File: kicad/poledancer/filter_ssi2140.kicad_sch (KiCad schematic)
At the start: 93 parts, among them U10 AS3364, U11 TL074, U12 SSI2140, U13 SSI2190, U14 TL074, U15 DG442xY, U3 TL074

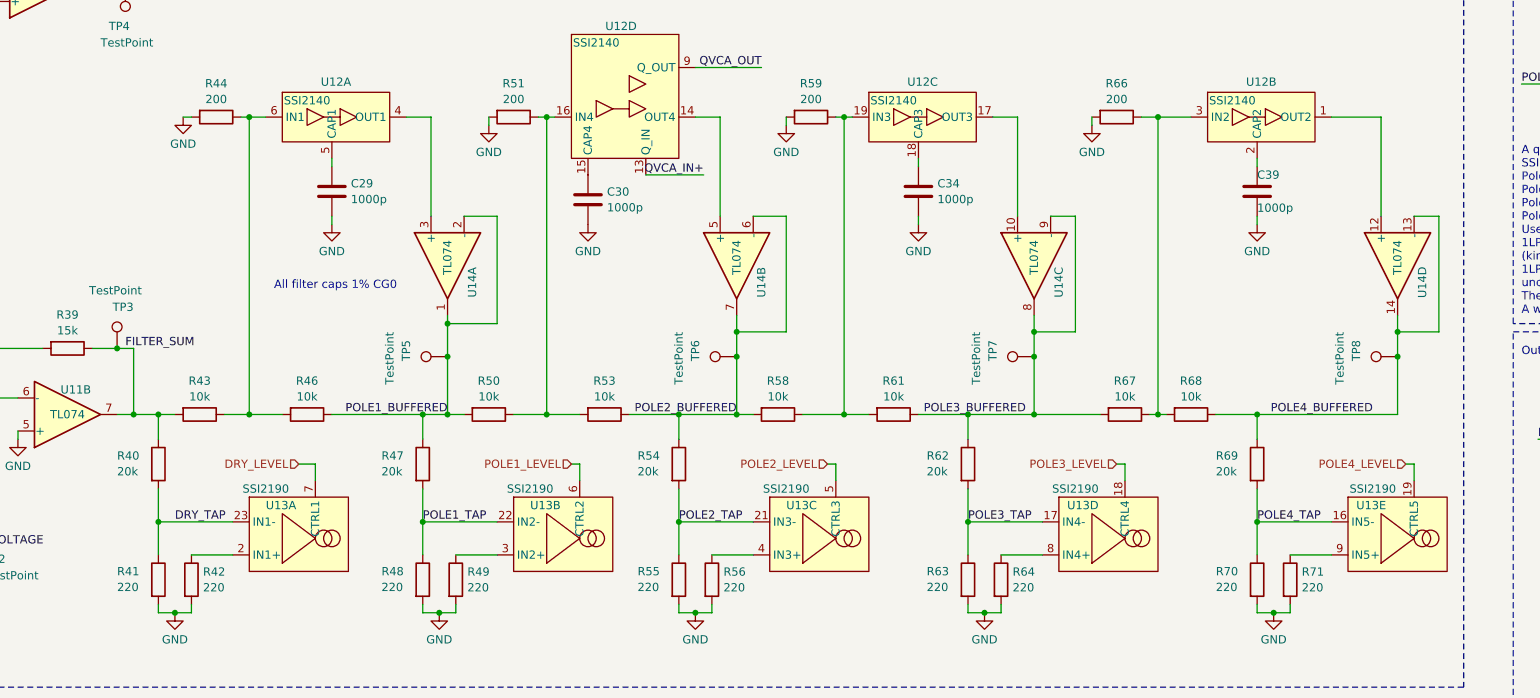
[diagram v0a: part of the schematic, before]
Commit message: create hand solder footprints for SSI chips.  Get some placement done.
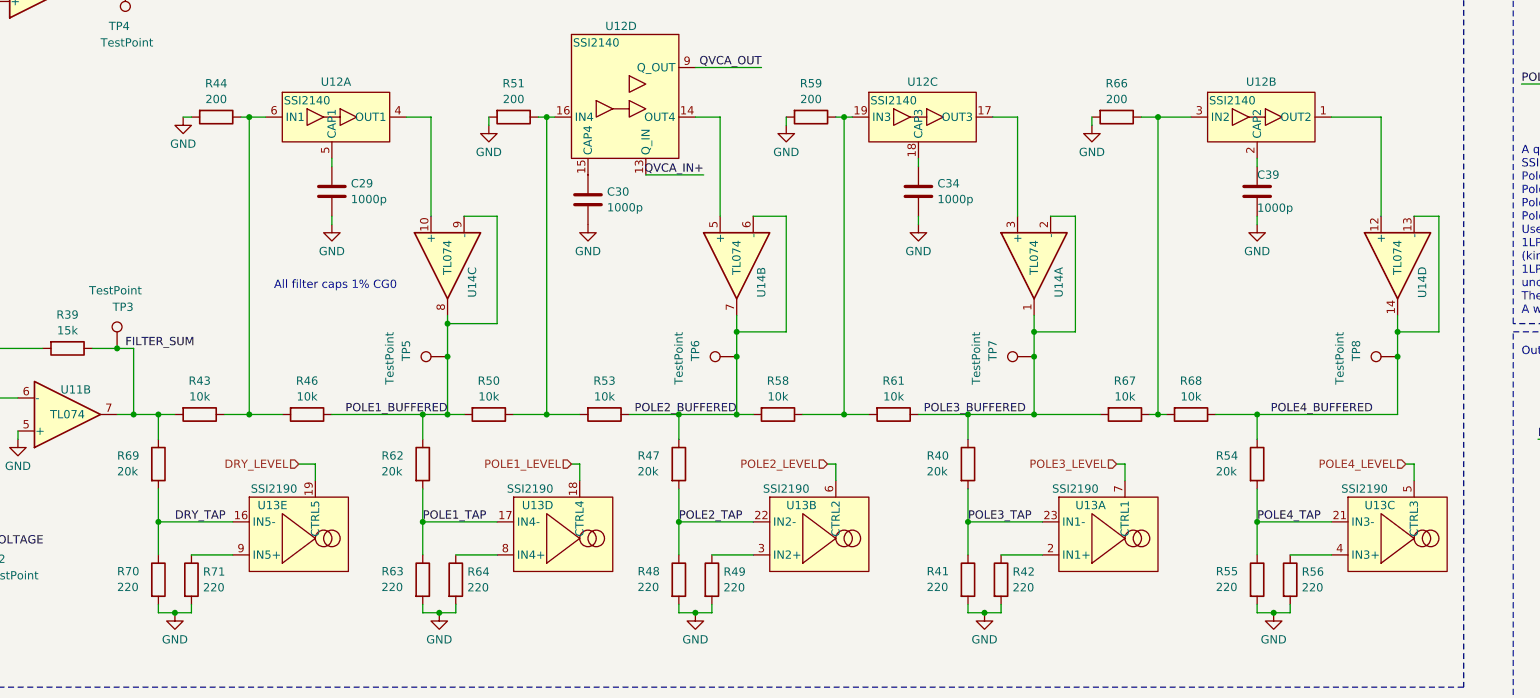
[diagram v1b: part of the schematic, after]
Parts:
- C29, C30, C34, C39: footprint Capacitor_SMD:C_1206_3216Metric -> Capacitor_SMD:C_0805_2012Metric; Digikey 311-1911-1-ND -> 478-KGM21BCG1H102FTCT-ND; Mfg CC1206FRNPO9BN102 -> KGM21BCG1H102FT
- U12: footprint Package_SO:SSOP-20_3.9x8.7mm_P0.635mm -> project_footprints:SSOP-20_3.9x8.7mm_P0.635mm_HandSolder
- U13: footprint Package_SO:SSOP-24_3.9x8.7mm_P0.635mm -> project_footprints:SSOP-24_3.9x8.7mm_P0.635mm_HandSolder
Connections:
- net DRY_LEVEL: now also U13.19 (CTRL5); no longer U13.7 (CTRL1)
- net DRY_TAP: now also R69.2, R70.1, U13.16 (IN5-); no longer R40.2, R41.1, U13.23 (IN1-)
- net FILTER_SUM: now also R69.1; no longer R40.1
- net POLE1_BUFFERED: now also R62.1, U14.8, U14.9 (-); no longer R47.1, U14.1, U14.2 (-)
- net POLE1_LEVEL: now also U13.18 (CTRL4); no longer U13.6 (CTRL2)
- net POLE1_TAP: now also R62.2, R63.1, U13.17 (IN4-); no longer R47.2, R48.1, U13.22 (IN2-)
- net POLE2_BUFFERED: now also R47.1; no longer R54.1
- net POLE2_LEVEL: now also U13.6 (CTRL2); no longer U13.5 (CTRL3)
- net POLE2_TAP: now also R47.2, R48.1, U13.22 (IN2-); no longer R54.2, R55.1, U13.21 (IN3-)
- net POLE3_BUFFERED: now also R40.1, U14.1, U14.2 (-); no longer R62.1, U14.8, U14.9 (-)
- net POLE3_LEVEL: now also U13.7 (CTRL1); no longer U13.18 (CTRL4)
- net POLE3_TAP: now also R40.2, R41.1, U13.23 (IN1-); no longer R62.2, R63.1, U13.17 (IN4-)
- net POLE4_BUFFERED: now also R54.1; no longer R69.1
- net POLE4_LEVEL: now also U13.5 (CTRL3); no longer U13.19 (CTRL5)
- net POLE4_TAP: now also R54.2, R55.1, U13.21 (IN3-); no longer R69.2, R70.1, U13.16 (IN5-)
- net at U12.4 (OUT1): now also U14.10 (+); no longer U14.3 (+)
- net at U12.17 (OUT3): now also U14.3 (+); no longer U14.10 (+)
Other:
- moved on the sheet: R40, R41, R42, R47, R48, R49, R54, R55, R56, R62, R63, R64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

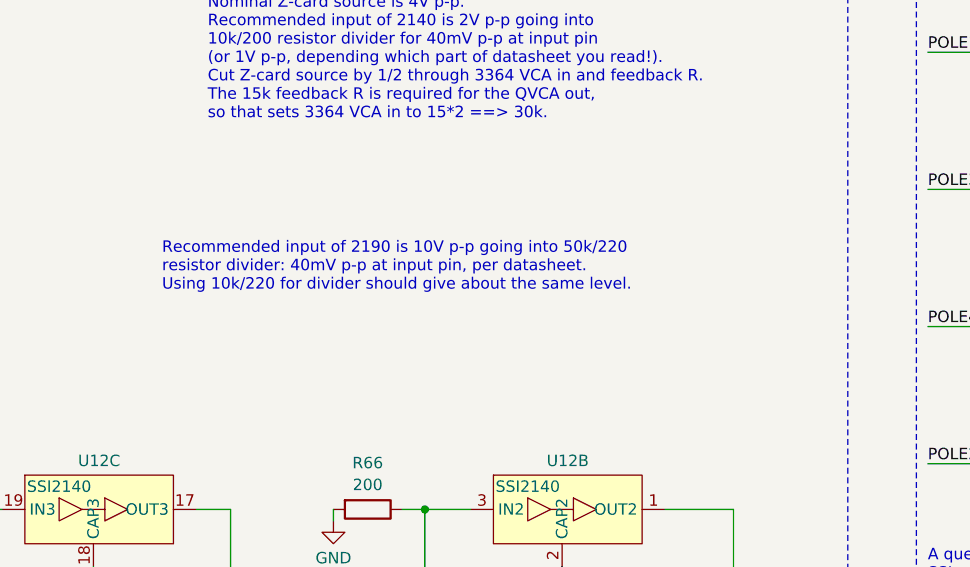
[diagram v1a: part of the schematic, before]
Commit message: checkpoint before changing some direction on this.  The resonance compensation is completely bonkers wrong.  Need to address that.
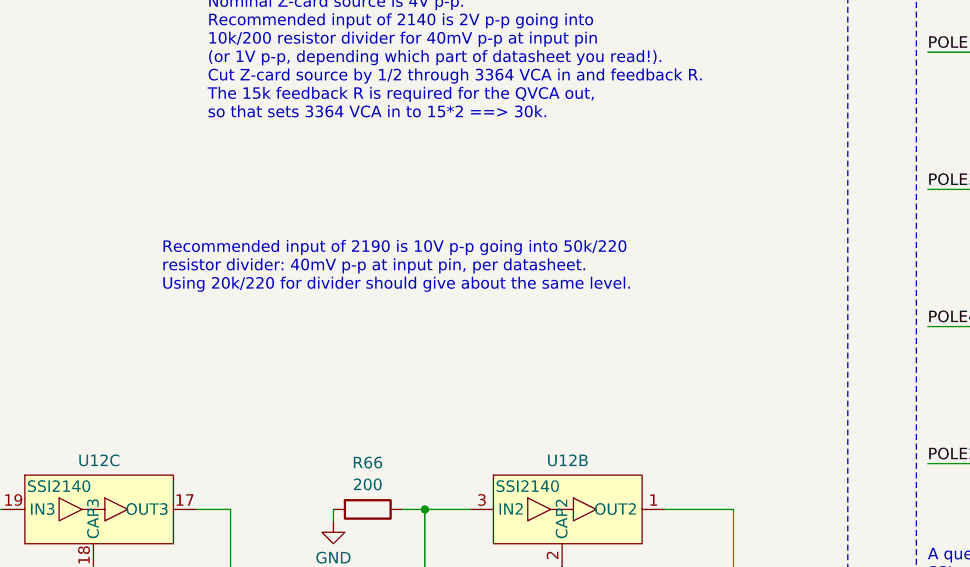
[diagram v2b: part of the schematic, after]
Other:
- note added: "Recommended input of 2190 is 10V p-p going into 50k/220 resistor divider: 40mV p-p at input pin, per datasheet. Using 20k/220 for divider should give about the same level."
- note removed: "Recommended input of 2190 is 10V p-p going into 50k/220 resistor divider: 40mV p-p at input pin, per datasheet. Using 10k/220 for divider should give about the same level."
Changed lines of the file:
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@@
     (effects (font (size 1.27 1.27)) (justify left bottom))
   )
-  (text "Recommended input of 2190 is 10V p-p going into 50k/220\nresistor divider: 40mV p-p at input pin, per datasheet.\nUsing 10k/220 for divider should give about the same level.\n"
+  (text "Recommended input of 2190 is 10V p-p going into 50k/220\nresistor divider: 40mV p-p at input pin, per datasheet.\nUsing 20k/220 for divider should give about the same level.\n"
     (at 234.95 52.07 0)
     (effects (font (size 1.27 1.27)) (justify left bottom))

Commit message: updated rez comp mode.  Back to placement on PCB.
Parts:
- removed R78: 20k, Resistor_SMD:R_0603_1608Metric, symbol Device:R
- R26: value 20k -> 15k; LCSC C4184 -> C22809
- R75: value 20k -> 10k; LCSC C4184 -> (none)
- U13: footprint project_footprints:SSOP-24_3.9x8.7mm_P0.635mm_HandSolder -> Package_SO:SSOP-24_3.9x8.7mm_P0.635mm
- renumbered R58 to R50, R50 to R58
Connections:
- net REZ_STAGE4_ENABLE is gone; now on net REZ_STAGE3_ENABLE: U15.16
- net GND: now also U11.12 (+); no longer R26.1, U11.5 (+)
- net POLE2_BUFFERED: now also R74.2
- net POLE3_BUFFERED: now also R75.2; no longer R74.2
- net POLE4_BUFFERED: no longer R75.2
- net QVCA_VOLTAGE: now also R26.2
- net REZ_STAGE2_ENABLE: now also U15.9; no longer U15.8
- net REZ_STAGE3_ENABLE: no longer U15.9
- net SOURCE1_AUDIO_LEVEL: now also U10.14 (Vc); no longer U10.3 (Vc)
- net SOURCE1_MOD_LEVEL: now also U10.3 (Vc); no longer U10.11 (Vc)
- net SOURCE2_AUDIO_LEVEL: now also U10.11 (Vc); no longer U10.6 (Vc)
- net SOURCE2_MOD_LEVEL: now also U10.6 (Vc); no longer U10.14 (Vc)
- net at U12.1 (OUT2): now also U14.5 (+); no longer U14.12 (+)
- net at U12.2 (CAP2): now also C30.1; no longer C39.1
- net at R66.1, R67.1, R68.2: now also U12.16 (IN4); no longer U12.3 (IN2)
- net at C28.1, R36.1, R38.2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: now also U10.4 (Iout), U10.5 (Iout); no longer U10.12 (Iout), U10.13 (Iout)
- net at R33.2: now also U10.15 (Iin); no longer U10.2 (Iin)
- net at U12.14 (OUT4): now also U14.12 (+); no longer U14.5 (+)
- net at R32.2: now also U10.7 (Iin); no longer U10.15 (Iin)
- net at U12.15 (CAP4): now also C39.1; no longer C30.1
- net at R34.2: now also U10.10 (Iin); no longer U10.7 (Iin)
- net at R37.1, R39.2, U11.6 (-): now also U10.12 (Iout), U10.13 (Iout); no longer U10.4 (Iout), U10.5 (Iout)
- net at R51.1, R53.2, R58.1: now also U12.3 (IN2); no longer U12.16 (IN4)
- net at R31.2: now also U10.2 (Iin); no longer U10.10 (Iin)
- new net: R26.1, U11.5 (+), U15.6
- new net QVCA_INVERT: U15.8
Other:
- note added: "A couple things on that opamp U11B... 15k is useful as the I-to-V for the 3364 VCA outputs. So 15k all around. The QVCA input can be switched phase based on the invert switch. This works as a summing only because the 3364 is current output, not voltage."
- note added: "A questionably weighted selection is used for resonance compensation. SSI app note AN701 details using SSI2164. This attempts the concept. Pole 1 switchable with a weight of 1. Pole 2 switchable with a weight of 1. Pole 3 switchable with a weight of 2. Pole 4 hardwired in the 2140 with a weight of 1. Used in conjuntion with QVCA_INVERT to phase correct the output. Useful combinations in the form 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"
- note added: "Sheet Vref load: 24k"
- note removed: "A questionably weighted selection is used for resonance compensation. SSI app note AN701 details using SSI2164. This attempts the concept. Pole 1 switchable with a weight of 1. Pole 2 switchable with a weight of 1. Pole 3 switchable with a weight of 1. Pole 4 switchable with a weight of 1. Useful combinations in the form (weight pole 1, 2, 3, 4): 1LP, 1HP: 1, 1, 0, 0 (REZ_STAGE1, STAGE2 set) (kin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"
- moved on the sheet: C30, C39, C42, C43, R35, R37, R73, R74, R75, TP2, U10B, U10C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

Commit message: continue placement
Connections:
- net FILTER_SUM: now also U11.1; no longer U11.7
- net GND: now also U11.5 (+); no longer U11.3 (+)
- net QVCA_OUT: now also U11.6 (-); no longer U11.2 (-)
- net QVCA_VOLTAGE: now also U11.7; no longer U11.1
- net at C28.1, R38.2, U10.4 (Iout)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: now also RV2.3; no longer R36.1
- net at R26.1, U15.6: now also U11.3 (+); no longer U11.5 (+)
- net at R37.1, R39.2, U10.12 (Iout)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: now also U11.2 (-); no longer U11.6 (-)
- net at C25.1, R27.1: now also R36.2; no longer RV2.1, RV2.2
- new net: R36.1, RV2.1, RV2.2
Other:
- moved on the sheet: R36, RV2, U11A, U11B
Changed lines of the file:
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@@
   (junction (at 336.55 181.61) (diameter 0) (color 0 0 0 0)
   )
-  (junction (at 63.5 24.13) (diameter 0) (color 0 0 0 0)
-  )
   (junction (at 154.94 113.03) (diameter 0) (color 0 0 0 0)
   )
@@
   (junction (at 260.35 243.84) (diameter 0) (color 0 0 0 0)
   )
+  (junction (at 71.12 24.13) (diameter 0) (color 0 0 0 0)
+  )
   (junction (at 153.67 152.4) (diameter 0) (color 0 0 0 0)
   )
@@
     (stroke (width 0) (type default))
   )
-  (wire (pts (xy 81.28 24.13) (xy 82.55 24.13))
+  (wire (pts (xy 80.01 24.13) (xy 82.55 24.13))
     (stroke (width 0) (type default))
   )
@@
     (stroke (width 0) (type default))
   )
-  (wire (pts (xy 72.39 24.13) (xy 73.66 24.13))
-    (stroke (width 0) (type default))
-  )
   (wire (pts (xy 238.76 224.79) (xy 238.76 223.52))
     (stroke (width 0) (type default))
@@
     (stroke (width 0) (type default))
   )
-  (wire (pts (xy 68.58 19.05) (xy 63.5 19.05))
+  (wire (pts (xy 76.2 19.05) (xy 71.12 19.05))
     (stroke (width 0) (type default))
   )
@@
     (stroke (width 0) (type default))
   )
-  (wire (pts (xy 68.58 20.32) (xy 68.58 19.05))
+  (wire (pts (xy 76.2 20.32) (xy 76.2 19.05))
     (stroke (width 0) (type default))
   )
@@
     (stroke (width 0) (type default))
   )
-  (wire (pts (xy 63.5 24.13) (xy 64.77 24.13))
+  (wire (pts (xy 71.12 24.13) (xy 72.39 24.13))
     (stroke (width 0) (type default))
   )
@@
     (stroke (width 0) (type default))
   )
-  (wire (pts (xy 63.5 19.05) (xy 63.5 24.13))
+  (wire (pts (xy 71.12 19.05) (xy 71.12 24.13))
     (stroke (width 0) (type default))
   )
@@
     (stroke (width 0) (type default))
   )
+  (wire (pts (xy 70.485 24.13) (xy 71.12 24.13))
+    (stroke (width 0) (type default))
+  )
   (wire (pts (xy 350.52 165.1) (xy 356.87 165.1))
     (stroke (width 0) (type default))
@@
     (stroke (width 0) (type default))
   )
-  (wire (pts (xy 34.29 209.55) (xy 36.83 209.55))
+  (wire (pts (xy 31.115 209.55) (xy 36.83 209.55))
     (stroke (width 0) (type default))
   )
@@
     (stroke (width 0) (type default))
   )
-  (wire (pts (xy 55.88 24.13) (xy 63.5 24.13))
+  (wire (pts (xy 55.88 24.13) (xy 62.865 24.13))
     (stroke (width 0) (type default))
   )
@@
     (effects (font (size 1.27 1.27)) (justify left bottom))
   )
-  (text "OFFSET" (at 34.925 218.44 0)
+  (text "OFFSET" (at 36.195 218.44 0)
     (effects (font (size 1.27 1.27)) (justify left bottom))
   )
@@
     (effects (font (size 1.27 1.27)) (justify left bottom))
   )
-  (text "SCALING" (at 65.405 33.02 0)
+  (text "SCALING" (at 71.12 33.02 0)
     (effects (font (size 1.27 1.27)) (justify left bottom))
   )
@@
     (effects (font (size 1.27 1.27)) (justify right))
   )
-  (hierarchical_label "V2.5_REF" (shape input) (at 34.29 209.55 180) (fields_autoplaced)
+  (hierarchical_label "V2.5_REF" (shape input) (at 31.115 209.55 180) (fields_autoplaced)
     (effects (font (size 1.27 1.27)) (justify right))
   )
@@
     )
   )
-  (symbol (lib_id "Amplifier_Operational:TL074") (at 51.435 142.24 0) (mirror x) (unit 1)
+  (symbol (lib_id "Amplifier_Operational:TL074") (at 96.52 121.92 0) (mirror x) (unit 1)
     (in_bom yes) (on_board yes) (dnp no)
-    (property "Reference" "U11" (at 53.975 138.43 0)
+    (property "Reference" "U11" (at 99.06 118.11 0)
       (effects (font (size 1.27 1.27)))
     )
-    (property "Value" "TL074" (at 50.165 142.24 0)
+    (property "Value" "TL074" (at 95.25 121.92 0)
       (effects (font (size 1.27 1.27)))
     )
-    (property "Footprint" "Package_SO:TSSOP-14_4.4x5mm_P0.65mm" (at 50.165 144.78 0)
+    (property "Footprint" "Package_SO:TSSOP-14_4.4x5mm_P0.65mm" (at 95.25 124.46 0)
       (effects (font (size 1.27 1.27)) hide)
     )
-    (property "Datasheet" "http://www.ti.com/lit/ds/symlink/tl071.pdf" (at 52.705 147.32 0)
+    (property "Datasheet" "http://www.ti.com/lit/ds/symlink/tl071.pdf" (at 97.79 127 0)
       (effects (font (size 1.27 1.27)) hide)
     )
-    (property "LCSC" "C96507" (at 51.435 142.24 0)
+    (property "LCSC" "C96507" (at 96.52 121.92 0)
       (effects (font (size 1.27 1.27)) hide)
     )
@@
     )
   )
-  (symbol (lib_id "Device:R") (at 77.47 24.13 270) (unit 1)
+  (symbol (lib_id "Device:R") (at 66.675 24.13 270) (unit 1)
     (in_bom yes) (on_board yes) (dnp no)
-    (property "Reference" "R36" (at 78.105 26.67 90)
+    (property "Reference" "R36" (at 67.31 26.67 90)
       (effects (font (size 1.27 1.27)))
     )
-    (property "Value" "27k" (at 78.105 29.21 90)
+    (property "Value" "27k" (at 67.31 29.21 90)
       (effects (font (size 1.27 1.27)))
     )
-    (property "Footprint" "Resistor_SMD:R_0603_1608Metric" (at 77.47 22.352 90)
+    (property "Footprint" "Resistor_SMD:R_0603_1608Metric" (at 66.675 22.352 90)
       (effects (font (size 1.27 1.27)) hide)
     )
-    (property "Datasheet" "~" (at 77.47 24.13 0)
+    (property "Datasheet" "~" (at 66.675 24.13 0)
       (effects (font (size 1.27 1.27)) hide)
     )
-    (property "LCSC" "C22967" (at 77.47 24.13 0)
+    (property "LCSC" "C22967" (at 66.675 24.13 0)
       (effects (font (size 1.27 1.27)) hide)
     )
@@
     )
   )
-  (symbol (lib_id "Amplifier_Operational:TL074") (at 96.52 121.92 0) (mirror x) (unit 2)
+  (symbol (lib_id "Amplifier_Operational:TL074") (at 51.435 142.24 0) (mirror x) (unit 2)
     (in_bom yes) (on_board yes) (dnp no)
-    (property "Reference" "U11" (at 97.79 118.11 0)
+    (property "Reference" "U11" (at 52.705 138.43 0)
       (effects (font (size 1.27 1.27)))
     )
-    (property "Value" "TL074" (at 96.52 121.92 0)
+    (property "Value" "TL074" (at 51.435 142.24 0)
       (effects (font (size 1.27 1.27)))
     )
-    (property "Footprint" "Package_SO:TSSOP-14_4.4x5mm_P0.65mm" (at 95.25 124.46 0)
+    (property "Footprint" "Package_SO:TSSOP-14_4.4x5mm_P0.65mm" (at 50.165 144.78 0)
       (effects (font (size 1.27 1.27)) hide)
     )
-    (property "Datasheet" "http://www.ti.com/lit/ds/symlink/tl071.pdf" (at 97.79 127 0)
+    (property "Datasheet" "http://www.ti.com/lit/ds/symlink/tl071.pdf" (at 52.705 147.32 0)
       (effects (font (size 1.27 1.27)) hide)
     )
-    (property "LCSC" "C96507" (at 96.52 121.92 0)
+    (property "LCSC" "C96507" (at 51.435 142.24 0)
       (effects (font (size 1.27 1.27)) hide)
     )
@@
     )
   )
-  (symbol (lib_id "Device:R_Potentiometer") (at 68.58 24.13 90) (unit 1)
+  (symbol (lib_id "Device:R_Potentiometer") (at 76.2 24.13 90) (unit 1)
     (in_bom yes) (on_board yes) (dnp no) (fields_autoplaced)
-    (property "Reference" "RV2" (at 68.58 26.8661 90)
+    (property "Reference" "RV2" (at 76.2 26.8661 90)
       (effects (font (size 1.27 1.27)))
     )
-    (property "Value" "5k" (at 68.58 29.2903 90)
+    (property "Value" "5k" (at 76.2 29.2903 90)
       (effects (font (size 1.27 1.27)))
     )
-    (property "Footprint" "Potentiometer_THT:Potentiometer_Bourns_3296W_Vertical" (at 68.58 24.13 0)
+    (property "Footprint" "Potentiometer_THT:Potentiometer_Bourns_3296W_Vertical" (at 76.2 24.13 0)
       (effects (font (size 1.27 1.27)) hide)
     )
-    (property "Datasheet" "~" (at 68.58 24.13 0)
+    (property "Datasheet" "~" (at 76.2 24.13 0)
       (effects (font (size 1.27 1.27)) hide)
     )
